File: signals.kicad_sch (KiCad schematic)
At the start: 43 parts

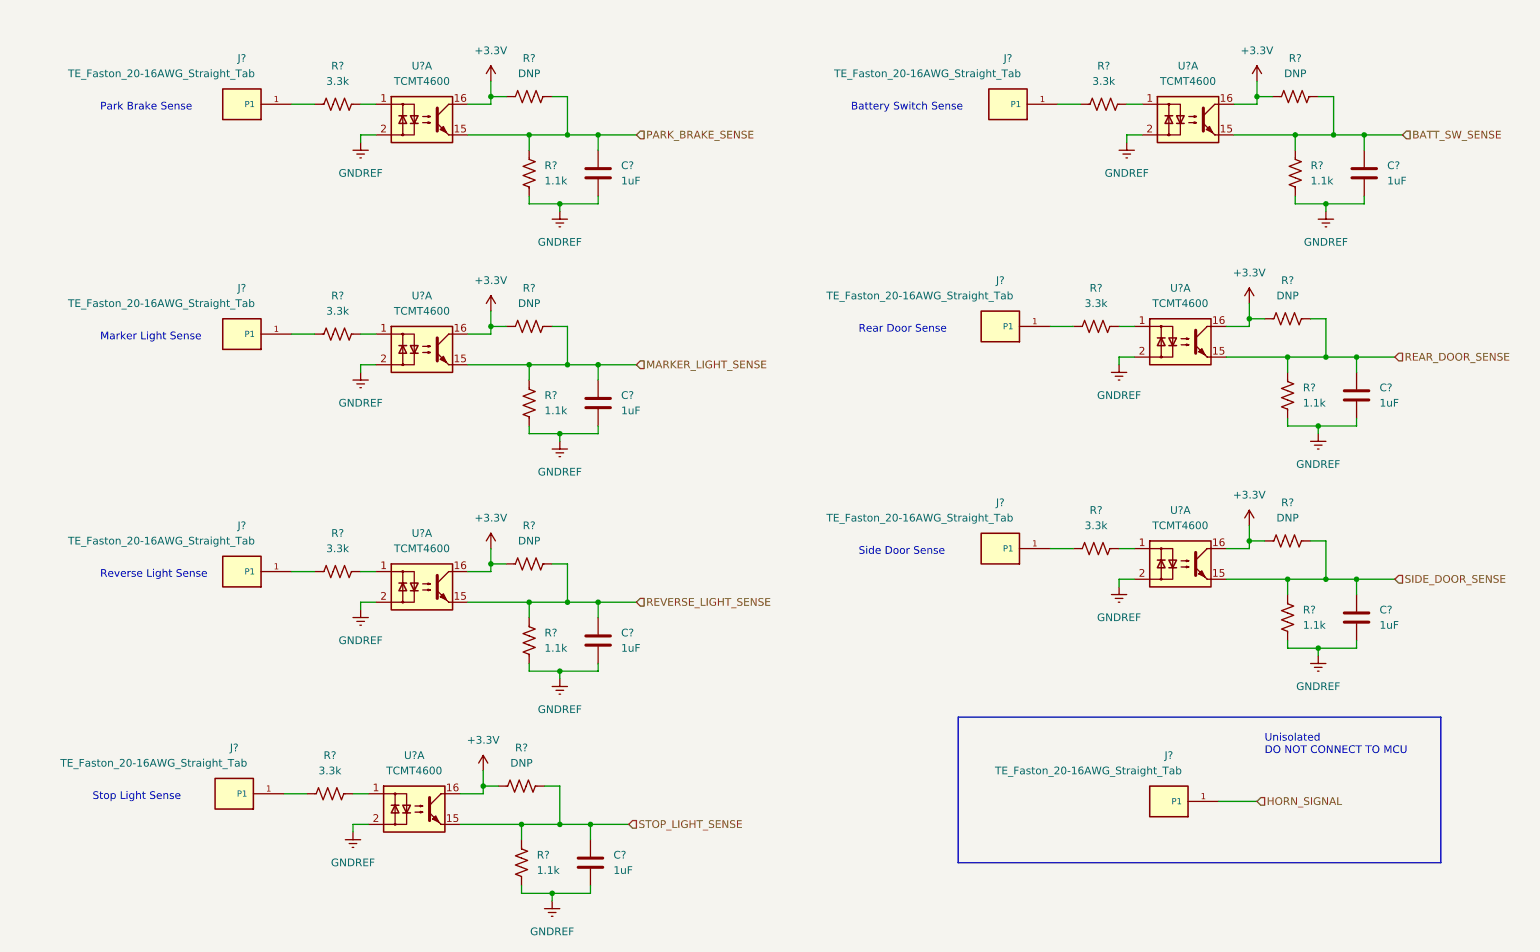
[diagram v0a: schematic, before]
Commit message: add horn sense
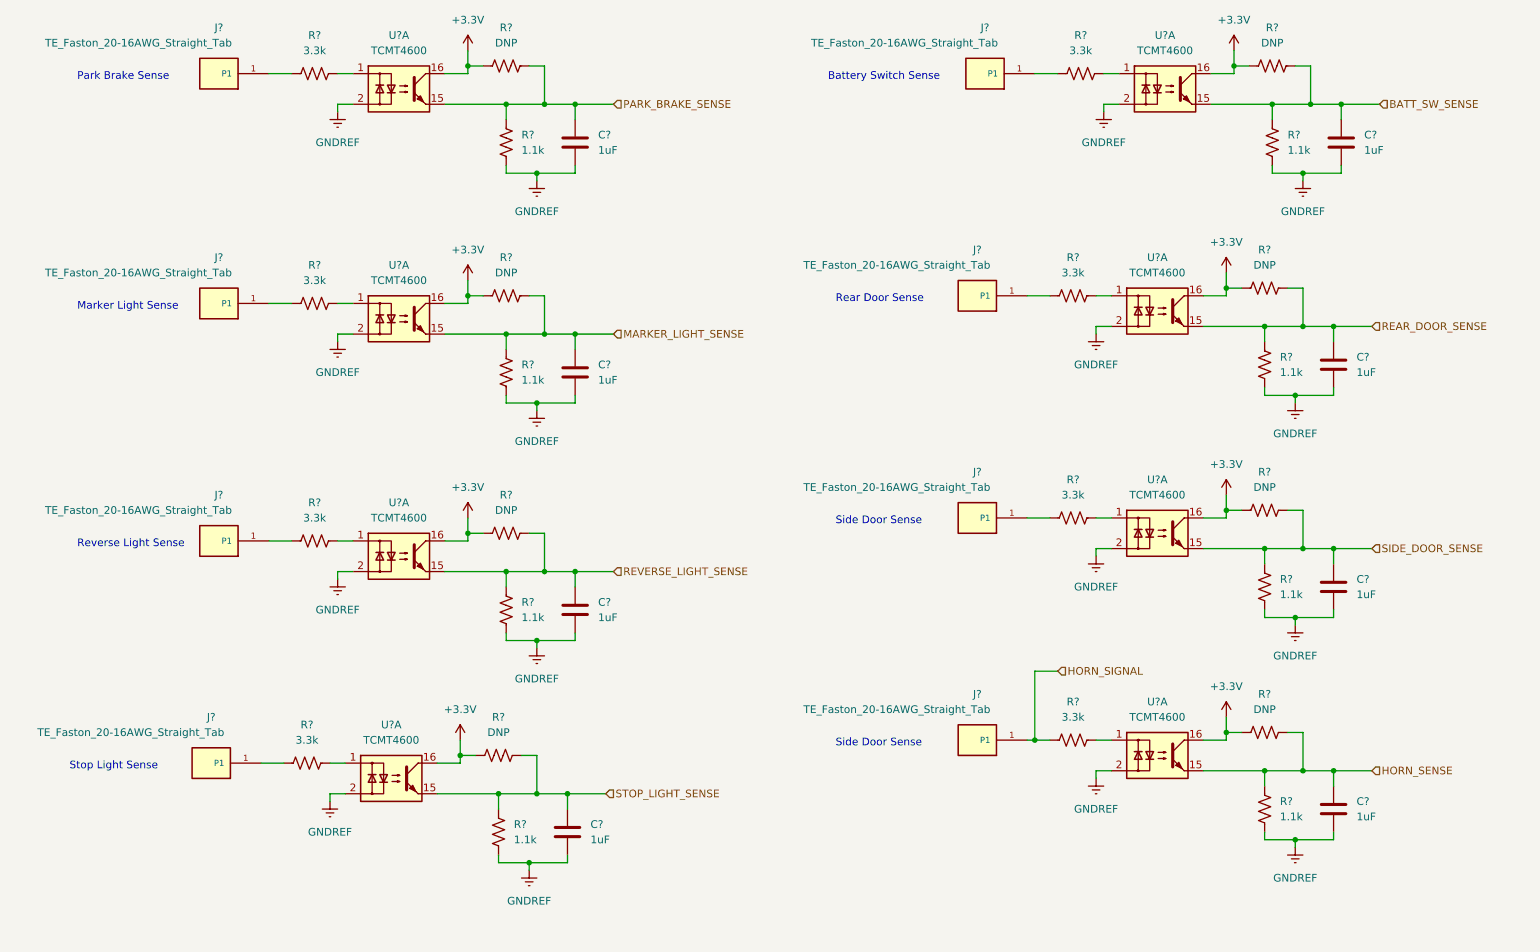
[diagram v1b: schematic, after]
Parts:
- removed J?: TE_Faston_20-16AWG_Straight_Tab, TE_Faston_20-16AWG_Straight_Tab, symbol Toadly:TE_Faston_20-16AWG_Straight_Tab
- added C?: 1uF, symbol Device:C
- added J?: TE_Faston_20-16AWG_Straight_Tab, TE_Faston_20-16AWG_Straight_Tab, symbol Toadly:TE_Faston_20-16AWG_Straight_Tab
- added R?: DNP, Resistor_SMD:R_0805_2012Metric_Pad1.20x1.40mm_HandSolder, symbol Device:R_US
- added R?: 1.1k, Resistor_SMD:R_0805_2012Metric_Pad1.20x1.40mm_HandSolder, symbol Device:R_US
- added R?: 3.3k, Resistor_SMD:R_0805_2012Metric_Pad1.20x1.40mm_HandSolder, symbol Device:R_US
- added U?: TCMT4600, Package_SO:SOP-16_4.55x10.3mm_P1.27mm, symbol Isolator:TCMT4600
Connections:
- net +3.3V: now also R?.2, U?.16
- net GNDREF: now also C?.2, R?.1, U?.2
- net HORN_SIGNAL: now also J?.1 (P1), J?.2 (P1), R?.1
- new net: R?.2, U?.1
- new net HORN_SENSE: C?.1, R?.1, R?.2, U?.15
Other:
- note removed: "Unisolated DO NOT CONNECT TO MCU"
- moved on the sheet: C?, J?, R?, U?A

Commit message: annotate schematic
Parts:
- C15, C16, C17, C18, C19, C20, C21, C22: renamed from C?; footprint (none) -> Capacitor_SMD:C_0805_2012Metric_Pad1.18x1.45mm_HandSolder
- gave numbers to parts that had none: 34
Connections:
- net +3.3V: now also U12.10, U12.12, U12.14, U13.10, U13.12, U13.14; no longer U12.16, U12.16, U12.16, U13.16, U13.16, U13.16
- net GNDREF: now also U12.4, U12.6, U12.8, U13.4, U13.6, U13.8; no longer U12.2, U12.2, U12.2, U13.2, U13.2, U13.2
- net HORN_SENSE: now also U13.9; no longer U13.15
- net MARKER_LIGHT_SENSE: now also U12.13; no longer U12.15
- net REAR_DOOR_SENSE: now also U13.13; no longer U13.15
- net REVERSE_LIGHT_SENSE: now also U12.11; no longer U12.15
- net SIDE_DOOR_SENSE: now also U13.11; no longer U13.15
- net STOP_LIGHT_SENSE: now also U12.9; no longer U12.15
- net at R25.2: now also U12.5; no longer U12.1
- net at R22.2: now also U12.7; no longer U12.1
- net at R34.2: now also U13.3; no longer U13.1
- net at R24.2: now also U12.3; no longer U12.1
- net at R36.2: now also U13.7; no longer U13.1
- net at R35.2: now also U13.5; no longer U13.1

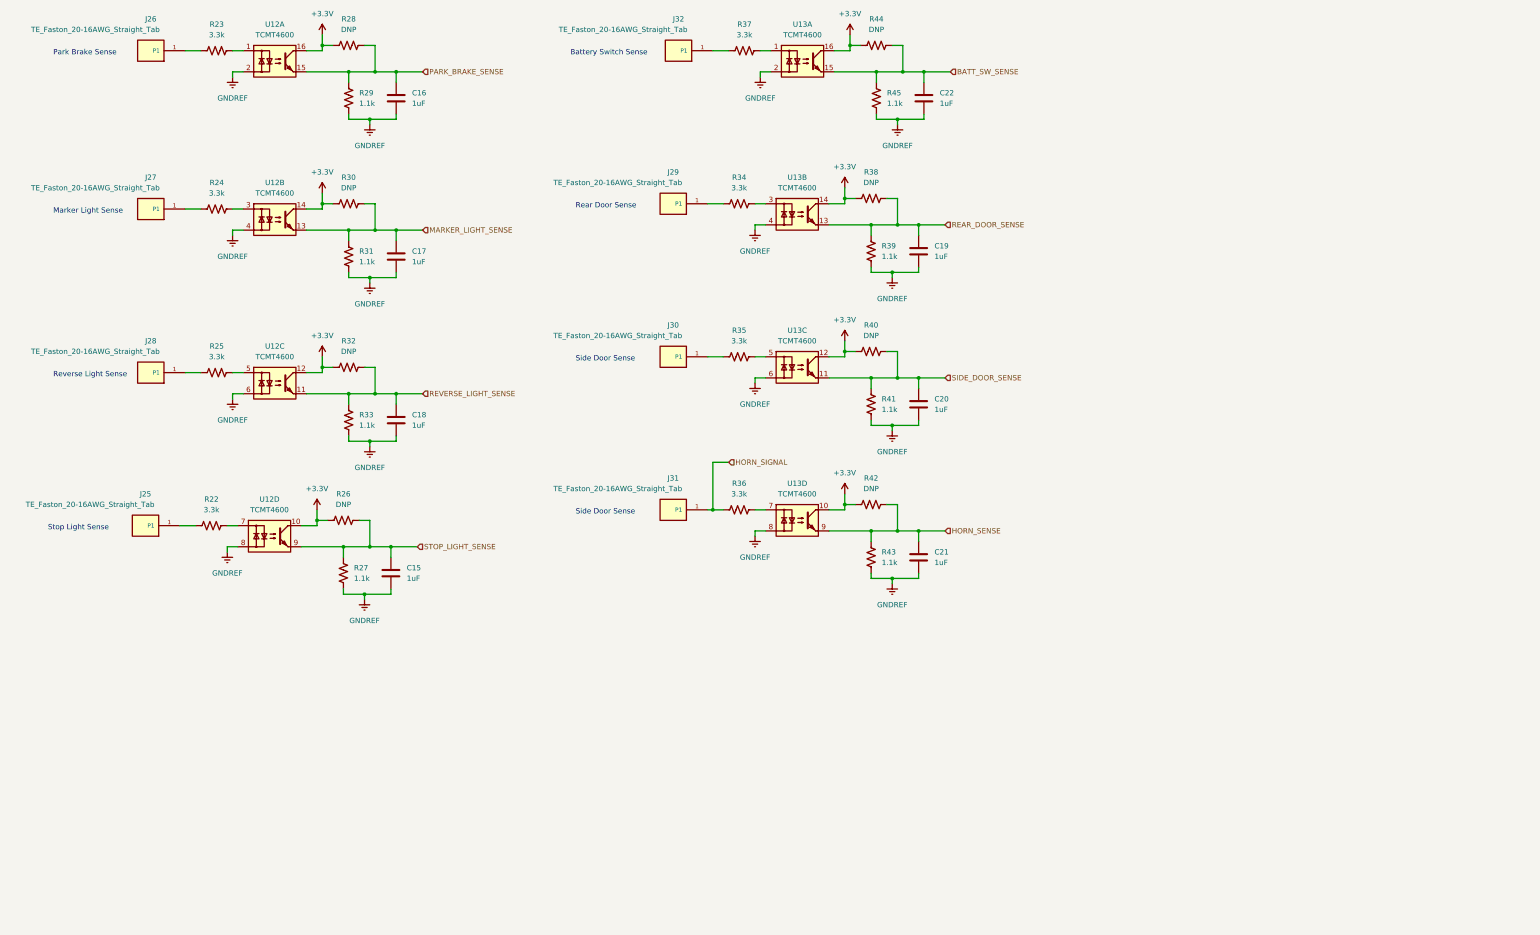
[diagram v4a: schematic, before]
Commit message: add compartment lights, switch to samd21j
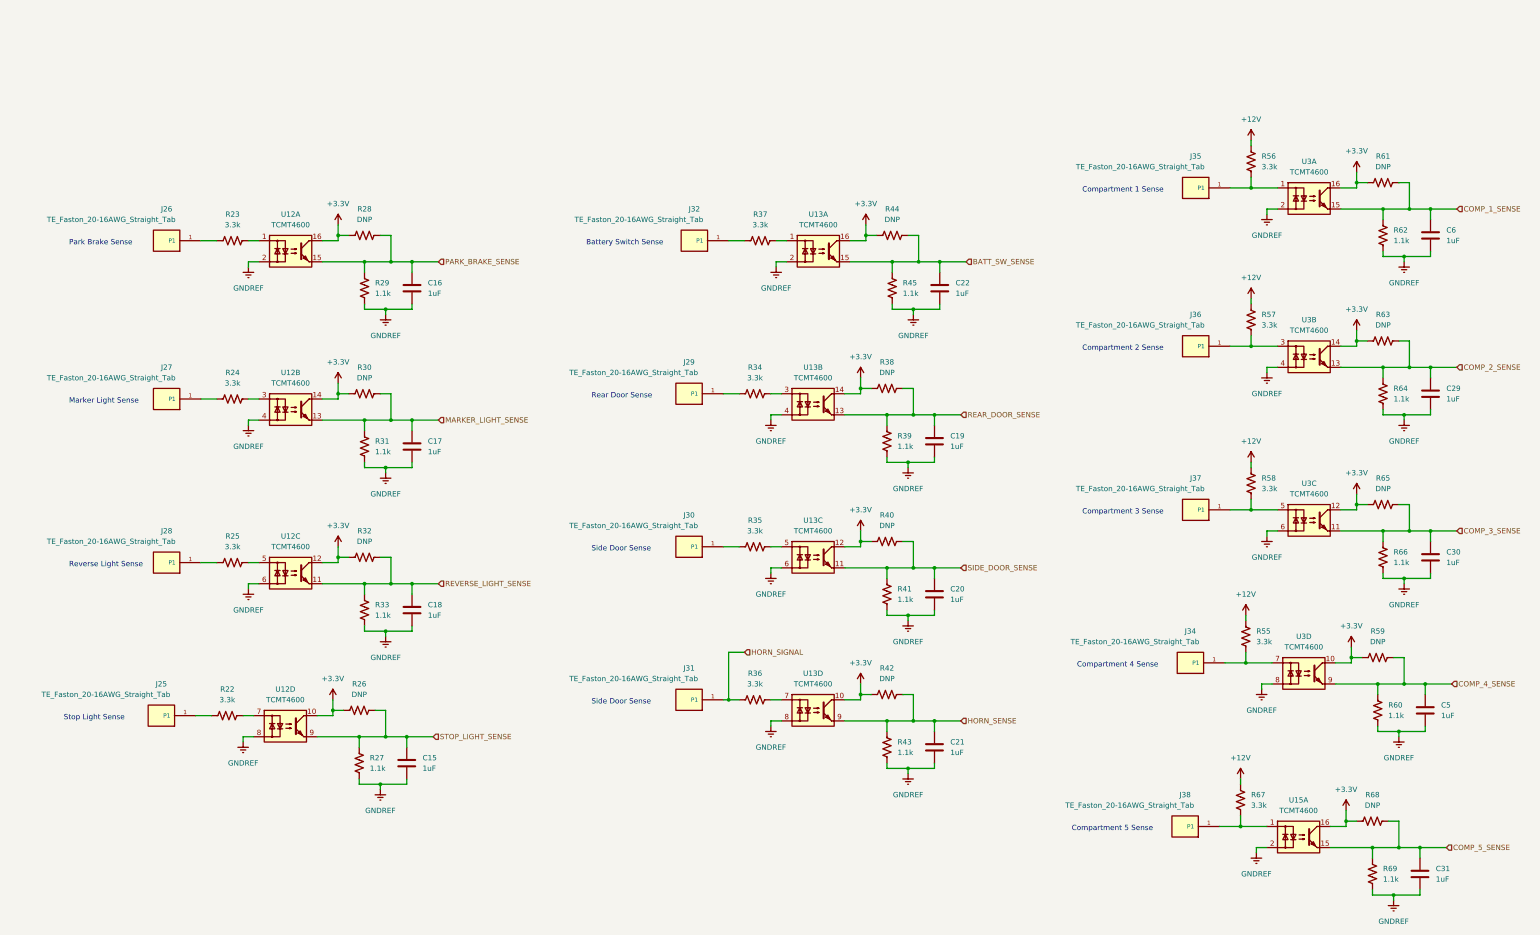
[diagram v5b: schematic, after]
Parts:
- added C29, C30, C31, C5, C6: 1uF, Capacitor_SMD:C_0805_2012Metric_Pad1.18x1.45mm_HandSolder, symbol Device:C
- added J34, J35, J36, J37, J38: TE_Faston_20-16AWG_Straight_Tab, TE_Faston_20-16AWG_Straight_Tab, symbol Toadly:TE_Faston_20-16AWG_Straight_Tab
- added R55, R56, R57, R58, R67: 3.3k, Resistor_SMD:R_0805_2012Metric_Pad1.20x1.40mm_HandSolder, symbol Device:R_US
- added R59, R61, R63, R65, R68: DNP, Resistor_SMD:R_0805_2012Metric_Pad1.20x1.40mm_HandSolder, symbol Device:R_US
- added R60, R62, R64, R66, R69: 1.1k, Resistor_SMD:R_0805_2012Metric_Pad1.20x1.40mm_HandSolder, symbol Device:R_US
- added U15, U3: TCMT4600, Package_SO:SOP-16_4.55x10.3mm_P1.27mm, symbol Isolator:TCMT4600
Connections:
- net +3.3V: now also R59.2, R61.2, R63.2, R65.2, R68.2, U15.16, U3.10, U3.12, U3.14, U3.16
- net GNDREF: now also C29.2, C30.2, C31.2, C5.2, C6.2, R60.1, R62.1, R64.1, R66.1, R69.1, U15.2, U3.2, U3.4, U3.6, U3.8
- new net: J34.1 (P1), J34.2 (P1), R55.1, U3.7
- new net: J35.1 (P1), J35.2 (P1), R56.1, U3.1
- new net: J37.1 (P1), J37.2 (P1), R58.1, U3.5
- new net: J36.1 (P1), J36.2 (P1), R57.1, U3.3
- new net: J38.1 (P1), J38.2 (P1), R67.1, U15.1
- new net +12V: R55.2, R56.2, R57.2, R58.2, R67.2
- new net COMP_1_SENSE: C6.1, R61.1, R62.2, U3.15
- new net COMP_2_SENSE: C29.1, R63.1, R64.2, U3.13
- new net COMP_3_SENSE: C30.1, R65.1, R66.2, U3.11
- new net COMP_4_SENSE: C5.1, R59.1, R60.2, U3.9
- new net COMP_5_SENSE: C31.1, R68.1, R69.2, U15.15
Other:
- note added: "Compartment 1 Sense"
- note added: "Compartment 2 Sense"
- note added: "Compartment 3 Sense"
- note added: "Compartment 4 Sense"
- note added: "Compartment 5 Sense"
- moved on the sheet: C15, C16, C17, C18, C19, C20, C21, C22, J25, J26, J27, J28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

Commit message: remove drivers
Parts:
- added C35, C36, C37: 1uF, Capacitor_SMD:C_0805_2012Metric_Pad1.18x1.45mm_HandSolder, symbol Device:C
- added J44, J45, J46: TE_Faston_20-16AWG_Straight_Tab, TE_Faston_20-16AWG_Straight_Tab, symbol Toadly:TE_Faston_20-16AWG_Straight_Tab
- added R79, R90, R91, R92: 3.3k, Resistor_SMD:R_0805_2012Metric_Pad1.20x1.40mm_HandSolder, symbol Device:R_US
- added R81, R83, R84, R85, R87, R89, R93, R94, R95, R96: DNP, Resistor_SMD:R_0805_2012Metric_Pad1.20x1.40mm_HandSolder, symbol Device:R_US
- added R82, R86, R88: 1.1k, Resistor_SMD:R_0805_2012Metric_Pad1.20x1.40mm_HandSolder, symbol Device:R_US
- added unit 4 of U15
- added U19: TCMT4600, Package_SO:SOP-16_4.55x10.3mm_P1.27mm, symbol Isolator:TCMT4600
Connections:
- net +12V: now also R79.2, R83.2, R84.2
- net +3.3V: now also R81.2, R85.2, R87.2, U15.10, U19.12, U19.14
- net COMP_5_SENSE: now also C35.1, C36.1, C37.1, R81.1, R82.2, R85.1, R86.2, R87.1, R88.2, U15.9, U19.11, U19.13
- net GNDREF: now also C35.2, C36.2, C37.2, R82.1, R86.1, R88.1, U15.8, U19.4, U19.6
- net at R55.1, U3.7: now also R96.1; no longer J34.1 (P1), J34.2 (P1)
- net at R56.1, U3.1: now also R93.1; no longer J35.1 (P1), J35.2 (P1)
- net at R58.1, U3.5: now also R95.1; no longer J37.1 (P1), J37.2 (P1)
- net at R57.1, U3.3: now also R94.1; no longer J36.1 (P1), J36.2 (P1)
- net at R67.1, U15.1: now also R89.1; no longer J38.1 (P1), J38.2 (P1)
- new net: J38.1 (P1), J38.2 (P1), R89.2
- new net: J34.1 (P1), J34.2 (P1), R96.2
- new net: R79.1, R90.1, U19.3
- new net: J46.1 (P1), J46.2 (P1), R92.2
- new net: J44.1 (P1), J44.2 (P1), R90.2
- new net: R84.1, R92.1, U19.5
- new net: J36.1 (P1), J36.2 (P1), R94.2
- new net: R83.1, R91.1, U15.7
- new net: J45.1 (P1), J45.2 (P1), R91.2
- new net: J37.1 (P1), J37.2 (P1), R95.2
- new net: J35.1 (P1), J35.2 (P1), R93.2
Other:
- note added: "AUX Sense 1"
- note added: "AUX Sense 2"
- note added: "AUX Sense 3"
- note added: "Standard 12V Inputs"
- moved on the sheet: C15, C16, C17, C18, C19, C20, C21, C22, C29, C30, C31, C5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

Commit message: add cab signals and connect inputs
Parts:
- added C10, C11, C12, C13, C14, C7, C8, C9: 1uF, Capacitor_SMD:C_0805_2012Metric_Pad1.18x1.45mm_HandSolder, symbol Device:C
- added R10, R16, R18, R48, R71, R77, R8, R80: 1.1k, Resistor_SMD:R_0805_2012Metric_Pad1.20x1.40mm_HandSolder, symbol Device:R_US
- added R11, R12, R15, R17, R19, R20, R3, R4, R47, R7, R70, R72, R73, R76, R78, R9: DNP, Resistor_SMD:R_0805_2012Metric_Pad1.20x1.40mm_HandSolder, symbol Device:R_US
- added R13, R14, R21, R46, R5, R6, R74, R75: 3.3k, Resistor_SMD:R_0805_2012Metric_Pad1.20x1.40mm_HandSolder, symbol Device:R_US
- added U4, U5: TCMT4600, Package_SO:SOP-16_4.55x10.3mm_P1.27mm, symbol Isolator:TCMT4600
- R84: value DNP -> 3.3k
- R90, R92: value 3.3k -> DNP
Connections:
- net +12V: now also R13.2, R14.2, R21.2, R46.2, R5.2, R6.2, R74.2, R75.2
- net +3.3V: now also R15.2, R17.2, R47.2, R7.2, R70.2, R76.2, R78.2, R9.2, U4.10, U4.12, U4.14, U4.16, U5.10, U5.12, U5.14, U5.16
- net COMP_5_SENSE: no longer C35.1, C36.1, C37.1, R81.1, R82.2, R85.1, R86.2, R87.1, R88.2, U15.9, U19.11, U19.13
- net GNDREF: now also C10.2, C11.2, C12.2, C13.2, C14.2, C7.2, C8.2, C9.2, R10.1, R16.1, R18.1, R48.1, R71.1, R77.1, R8.1, R80.1, U4.2, U4.4, U4.6, U4.8, U5.2, U5.4, U5.6, U5.8
- net HORN_SENSE: now also C19.1, R38.1, R39.2, U13.13; no longer C21.1, R42.1, R43.2, U13.9
- net REAR_DOOR_SENSE: now also C35.1, R81.1, R82.2, U19.13; no longer C19.1, R38.1, R39.2, U13.13
- net SIDE_DOOR_SENSE: now also C37.1, R87.1, R88.2, U19.11; no longer C20.1, R40.1, R41.2, U13.11
- net HORN_SIGNAL: no longer names the net of J31.1 (P1), J31.2 (P1), R36.1
- new net: R12.1, R14.1, U4.5
- new net: R73.1, R75.1, U5.5
- new net: R11.1, R13.1, U4.7
- new net: R72.1, R74.1, U5.7
- new net: R20.1, R46.1, U5.1
- new net: R4.1, R6.1, U4.1
- new net: R3.1, R5.1, U4.3
- new net: R19.1, R21.1, U5.3
- new net AUX_1_SENSE: C20.1, R40.1, R41.2, U13.11
- new net AUX_2_SENSE: C21.1, R42.1, R43.2, U13.9
- new net AUX_3_SENSE: C36.1, R85.1, R86.2, U15.9
- new net CAB_1_SENSE: C8.1, R10.2, R9.1, U4.15
- new net CAB_2_SENSE: C7.1, R7.1, R8.2, U4.13
- new net CAB_3_SENSE: C10.1, R17.1, R18.2, U4.11
- new net CAB_4_SENSE: C9.1, R15.1, R16.2, U4.9
- new net CAB_5_SENSE: C12.1, R70.1, R71.2, U5.15
- new net CAB_6_SENSE: C11.1, R47.1, R48.2, U5.13
- new net CAB_7_SENSE: C14.1, R78.1, R80.2, U5.11
- new net CAB_8_SENSE: C13.1, R76.1, R77.2, U5.9
- new net CAB_SIGNAL_1: R4.2
- new net CAB_SIGNAL_2: R3.2
- new net CAB_SIGNAL_3: R12.2
- new net CAB_SIGNAL_4: R11.2
- new net CAB_SIGNAL_5: R20.2
- new net CAB_SIGNAL_6: R19.2
- new net CAB_SIGNAL_7: R73.2
- new net CAB_SIGNAL_8: R72.2
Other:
- note added: "Aux 1 Sense"
- note added: "Aux 2 Sense"
- note added: "Horn Sense"
- note removed: "AUX Sense 1"
- note removed: "AUX Sense 2"
- moved on the sheet: C29, C30, C31, C35, C36, C37, C5, C6, J34, J35, J36, J37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

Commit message: connect signals to connectors, start layout
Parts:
- renumbered C15 to C11, C16 to C12, C17 to C13, C18 to C14, C7 to C15, C8 to C16, C19 to C17, C20 to C18, C21 to C19, C22 to C20, C9 to C21, C10 to C22, C11 to C23, C12 to C24, C35 to C25, C31 to C26, C6 to C27, C29 to C28, C13 to C29, C14 to C30, C36 to C31, C37 to C32, C5 to C33, C30 to C34, J25 to J12, J26 to J13, J27 to J14, J28 to J15, J29 to J16, J30 to J17, J31 to J18, J32 to J19, J35 to J20, J36 to J21, J44 to J22, J38 to J23, J45 to J24, J46 to J25, J34 to J26, J37 to J27, R23 to R10, R24 to R11, R25 to R12, R3 to R13, R4 to R14, R5 to R15, R6 to R16, R26 to R17, R27 to R18, R28 to R19, R29 to R20, R30 to R21, R31 to R22, R32 to R23, R33 to R24, R7 to R25, R8 to R26, R9 to R27, R10 to R28, R34 to R29, R35 to R30, R36 to R31, R37 to R32, R11 to R33, R12 to R34, R13 to R35, R14 to R36, R38 to R37, R39 to R38, R40 to R39, R41 to R40, R42 to R41, R43 to R42, R44 to R43, R45 to R44, R15 to R45, R16 to R46, R17 to R47, R18 to R48, R19 to R49, R20 to R50, R90 to R51, R93 to R52, R94 to R53, R89 to R54, R21 to R55, R46 to R56, R79 to R57, R67 to R58, R56 to R59, R57 to R60, R47 to R61, R48 to R62, R70 to R63, R71 to R64, R81 to R65, R82 to R66, R68 to R67, R69 to R68, R61 to R69, R62 to R70, R63 to R71, R64 to R72, R72 to R73, R73 to R74, R91 to R75, R92 to R76, R74 to R77, R75 to R78, R96 to R79, R95 to R80, R83 to R81, R84 to R82, R55 to R83, R58 to R84, R76 to R85, R77 to R86, R78 to R87, R80 to R88, R85 to R89, R22 to R9, R86 to R90, R87 to R91, R88 to R92, R59 to R93, R60 to R94, R65 to R95, R66 to R96, U12 to U4, U4 to U5, U13 to U6, U5 to U7, U19 to U8, U15 to U8, U3 to U9
